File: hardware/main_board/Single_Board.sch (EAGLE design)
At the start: 37 parts, among them J1 5520425-3, J2 U.FL, J3 AVR_SPI_PROG_3X2NS, Q1 200mA/40V, Q2 220mA/50V/3.5Ω, U2 MCP1703T-3302E/CB, U3 W25X40CLSNIG, U5 ATMEGA328PB-AU, X1 32.768KHZ-FC-135, X2 B2B-PH-K-S, X3 B2B-XH-2

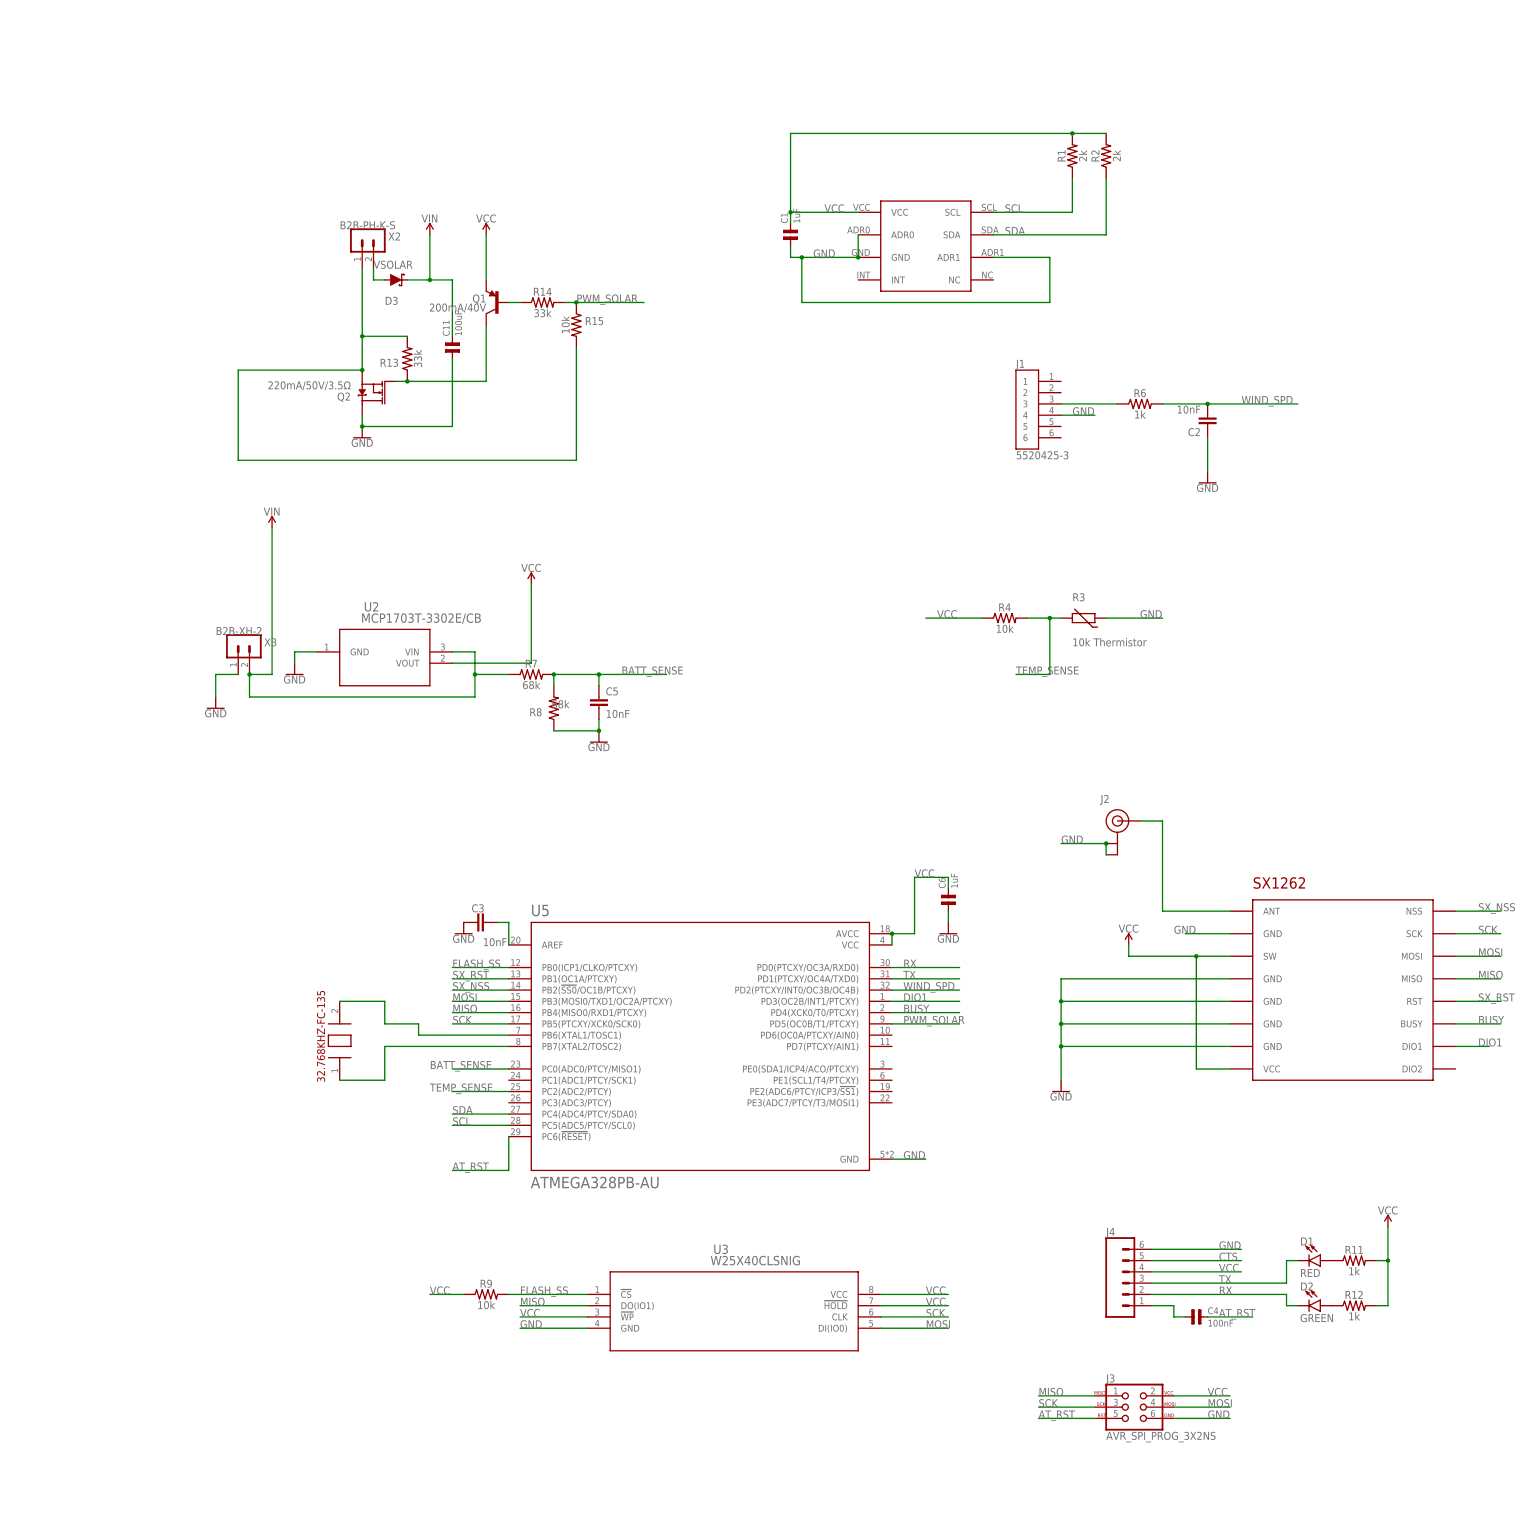
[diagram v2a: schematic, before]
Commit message: Added daylight indicators
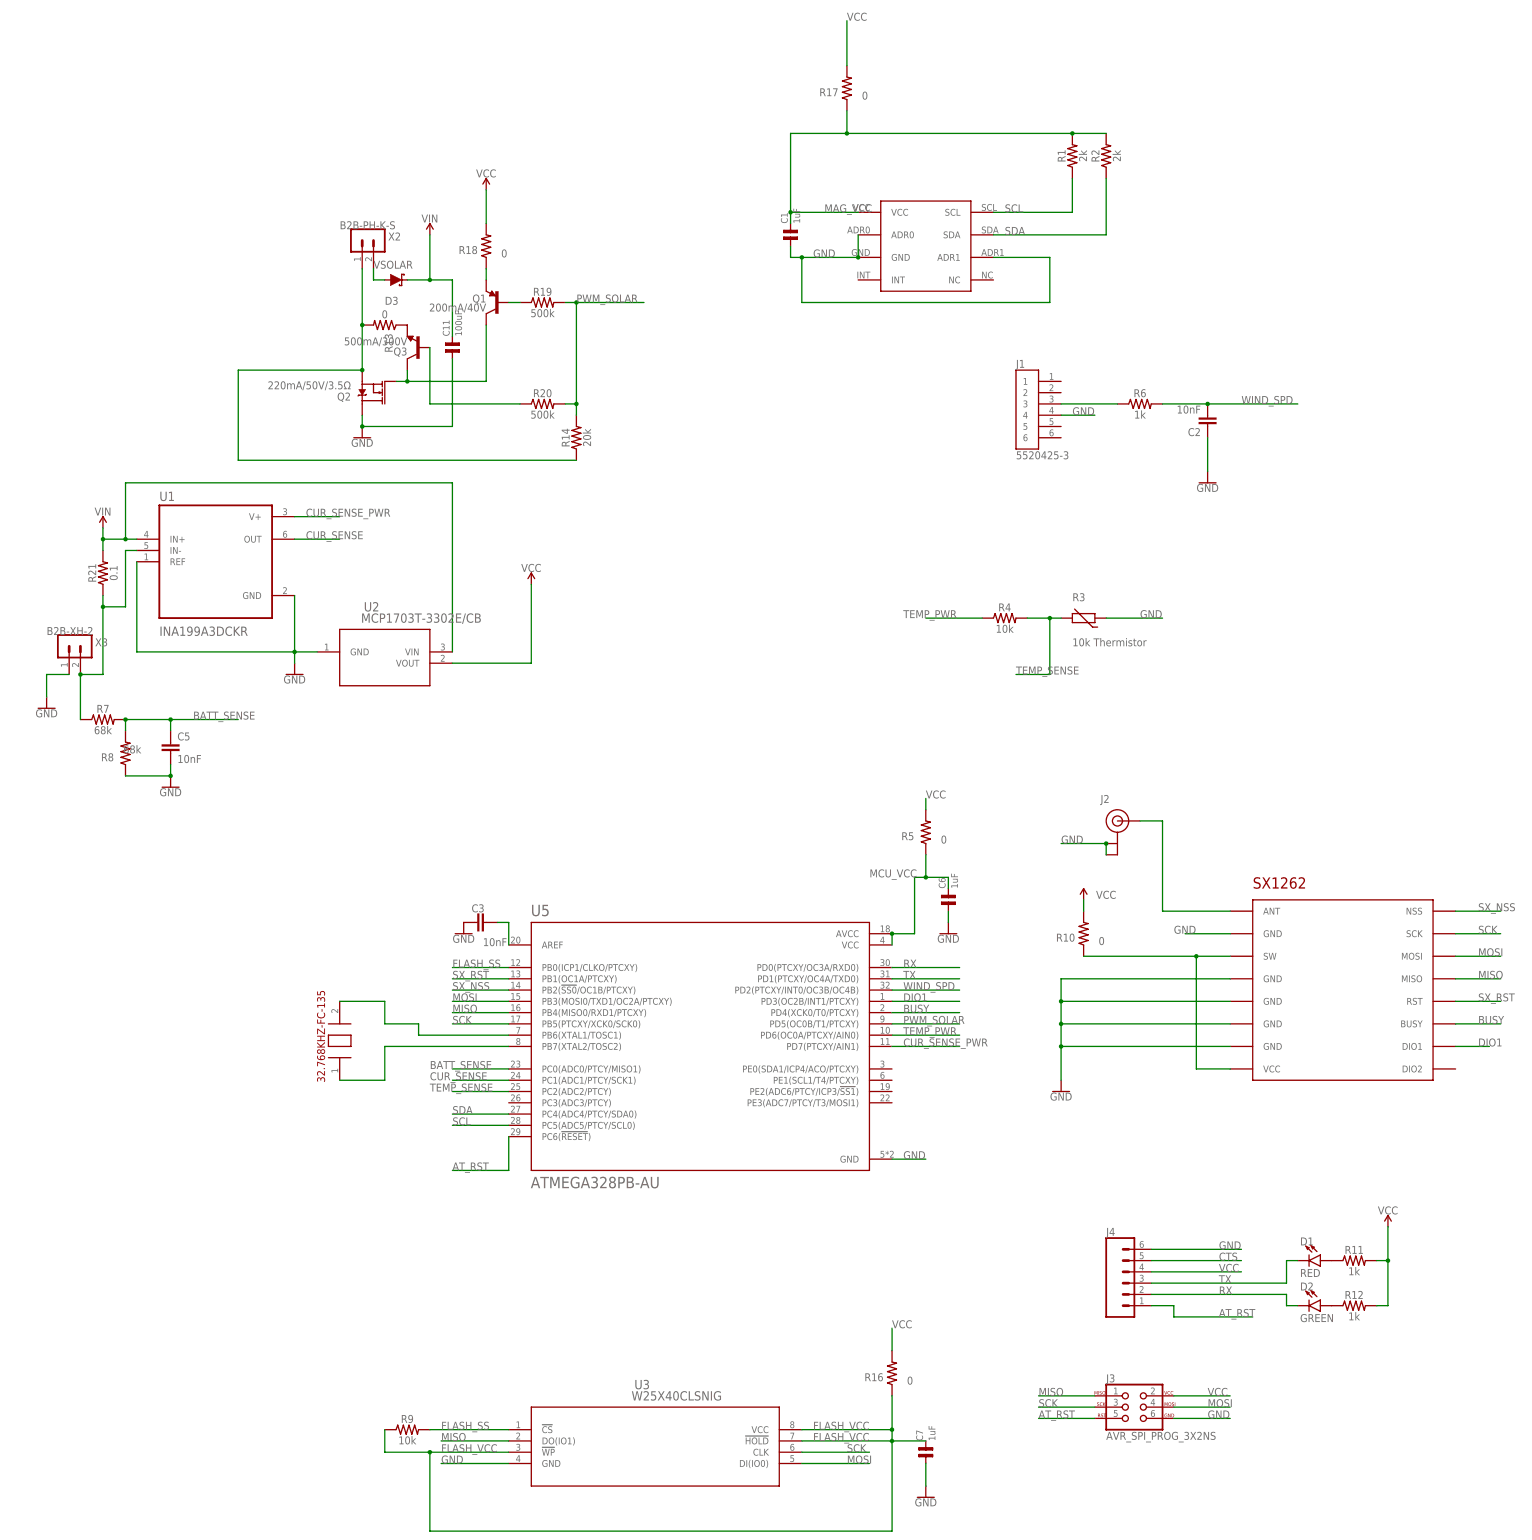
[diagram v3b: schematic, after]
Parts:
- removed C4: 100nF, main_board:C0805
- removed R15: 10k, SparkFun-Resistors:RESISTOR0805
- added C7: 1uF, capsmd:C0805
- added Q3: 500mA/300V, SparkFun-DiscreteSemi:TRANS_NPN-MMBTA42
- added R10, R16, R17, R18, R5: 0, SparkFun-Resistors:RESISTOR0805
- added R19, R20: 500k, SparkFun-Resistors:RESISTOR0402
- added R21: 0.1, SparkFun-Resistors:RESISTOR1206
- added U1: INA199A3DCKR, main_board:INA199A3DCKR
- R13: value 33k -> 0
- R14: value 33k -> 20k; device SparkFun-Resistors:RESISTOR0805 -> SparkFun-Resistors:RESISTOR0402
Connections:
- new net CUR_SENSE: U1.OUT, U5.PC1(ADC1/PTCY/SCK1)
- new net CUR_SENSE_PWR: U1.V+, U5.PD7(PTCXY/AIN1)
- new net FLASH_VCC: C7.2, R16.1, R9.1, U3.!HOLD, U3.!WP, U3.VCC
- new net MAG_VCC: C1.2, R1.2, R17.1, R2.2, U$1.VCC
- new net MCU_VCC: C6.2, R5.1, U5.AVCC, U5.VCC
- new net N$1: R10.1, U$2.SW, U$2.VCC
- new net N$10: Q3.B, R20.1
- new net N$3: Q1.E, R18.1
- new net N$5: Q3.E, R13.1
- new net TEMP_PWR: R4.1, U5.PD6(OC0A/PTCXY/AIN0)
- net AT_RST: now also J4.1; no longer C4.2
- net GND: now also C7.1, U1.GND, U1.REF
- net N$11: now also R21.1, R7.1, U1.IN-, X3.2; no longer C4.1, J4.1
- net N$12: now also Q3.C; no longer R13.1
- net N$13: now also R19.1; no longer R14.1
- net N$9: now also R14.1; no longer R15.2
- net PWM_SOLAR: now also R19.2, R20.2; no longer R15.1
- net VCC: now also R10.2, R16.2, R17.2, R18.2, R5.2; no longer C1.2, C6.2, Q1.E, R1.2, R2.2, R4.1, R9.1, U$1.VCC, U$2.SW, U$2.VCC, U3.!HOLD, U3.!WP, U3.VCC, U5.AVCC, U5.VCC
- net VIN: now also R21.2, U1.IN+; no longer R7.1, X3.2
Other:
- moved on the sheet: C5, R13, R14, R7, R8, R9, U3, X3

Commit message: Station improvements. Multi-subpacket handling in receiver. Out of order packets in site datamanager.
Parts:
- removed Q3: 500mA/300V, SparkFun-DiscreteSemi:TRANS_NPN-MMBTA42
- removed R19, R20: 500k, SparkFun-Resistors:RESISTOR0402
- added C4, C8: 10nF, SparkFun-Capacitors:10NF-0603-50V-10%
- added C9: 1uF, capsmd:C0805
- added R15: 10k, SparkFun-Resistors:RESISTOR0805
- Q1: value 200mA/40V -> 220mA/50V/3.5Ω; device SparkFun-DiscreteSemi:TRANS_PNP-PMBT3906|MMBT3906L -> SparkFun-DiscreteSemi:MOSFET-NCH-BSS138
- R13: value 0 -> 200
- R14: value 20k -> 6k; device SparkFun-Resistors:RESISTOR0402 -> SparkFun-Resistors:RESISTOR0805
- R18: value 0 -> 42k
- R7, R8: value 68k -> 220k
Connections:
- removed net N$12: Q1.C, Q2.G, Q3.C
- removed net N$13: Q1.B, R19.1
- net CUR_SENSE: now also C8.2, R18.1; no longer U1.OUT
- net CUR_SENSE_PWR: now also C9.2
- net GND: now also C4.1, C8.1, C9.1
- net N$10: now also Q1.D, Q2.G, R15.1; no longer Q3.B, R20.1
- net N$3: now also Q1.S, R13.1; no longer Q1.E, R18.1
- net N$5: now also R18.2, U1.OUT; no longer Q3.E, R13.1
- net N$9: now also R14.2; no longer R14.1
- net PWM_SOLAR: now also Q1.G, R14.1; no longer R14.2, R19.2, R20.2
- net TEMP_SENSE: now also C4.2
- net VCC: now also R15.2; no longer R18.2
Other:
- moved on the sheet: C11, D3, R14, R18
